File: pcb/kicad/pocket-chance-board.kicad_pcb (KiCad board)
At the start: 4 copper layers, 150 x 100 mm, 132 parts, among them J1 SWD, J2 USB4085-GF-A, J3 LiPo JST-PH 2.0mm (1 = + RED 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, J4 LCD 1.54in ST7789 module, JST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, J5 Speaker JST-PH, J6 microSD Molex 104031-0811, J7 STEMMA QT, J8 Expansion (6 = VBAT_SENSE ADC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, Q1 FS8205A, Q3 AO3400A, Q4 AO3401A, SW1 BOOT, SW10 DPAD LEFT PTS645SM43SMTR92, SW11 DPAD RIGHT PTS645SM43SMTR92, SW12 DPAD PRESS PTS645SM43SMTR92, SW2 RESET, SW3 POWER PCM12, SW4 A PTS125SM43SMTR2LFS, SW5 B PTS125SM43SMTR2LFS, SW6 X PTS125SM43SMTR2LFS, SW7 Y PTS125SM43SMTR2LFS, SW8 DPAD UP PTS645SM43SMTR92, SW9 DPAD DOWN PTS645SM43SMTR92, U1 RP2350A, U10 LSM6DSOXTR, U11 RM2, U2 W25Q128JVSIQ, U3 APS6404L-3SQR-SN, U4 USBLC6-2SC6, U5 BQ24074RGTR, U6 TPS63001DRCR, U7 DW01A, U8 PAM8302AADCR, U9 DS3231MZ+, Y1 12MHz ABM8-272-T3

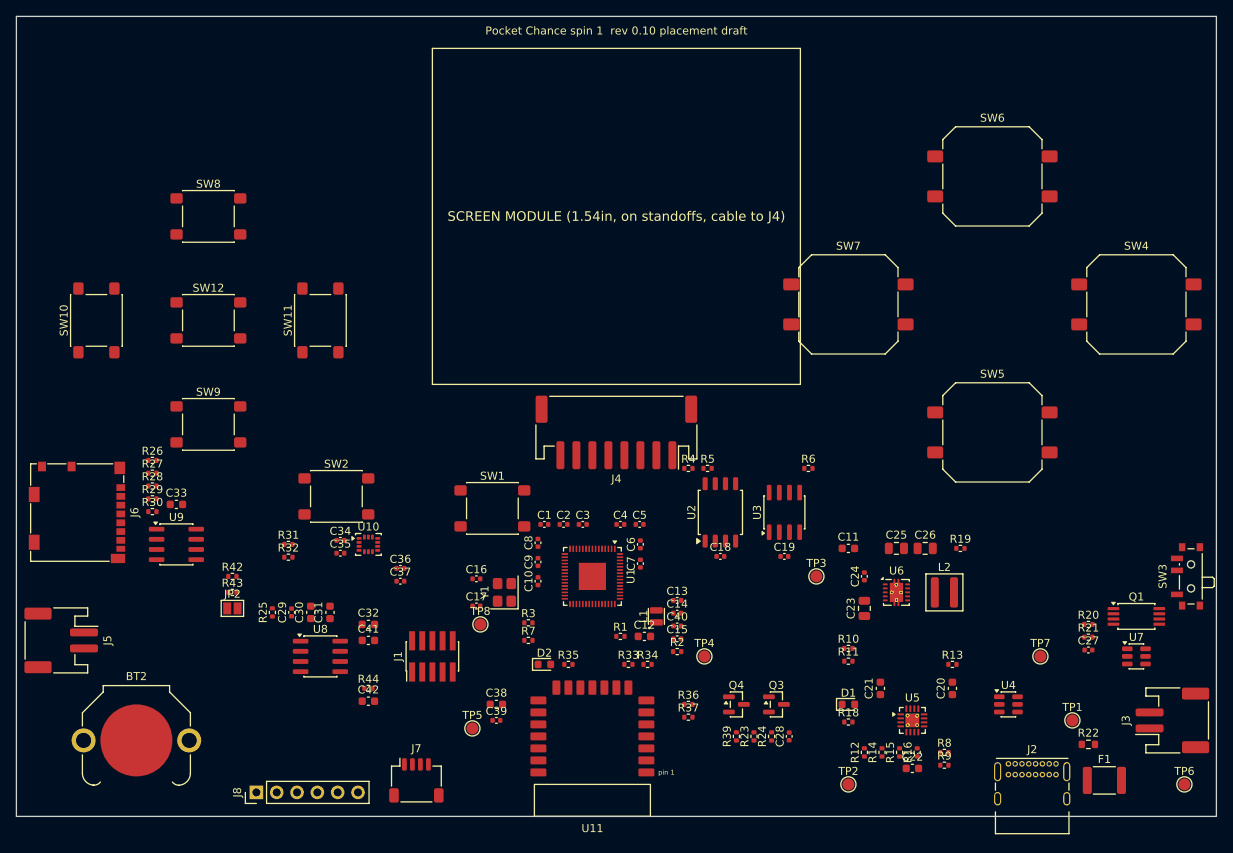
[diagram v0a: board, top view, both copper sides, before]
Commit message: Layout: placement pass 2 after the auditor's and expert's placement reviews
- RM2 keep-out rule area on all four copper layers (*.Cu), not F&B only
- U6 buck-boost repacked: L2 against the switch pins, VIN/VOUT caps on their pins
- RP2350 core regulator: L1/C13 within 1.5-2.6 mm of LX/VIN; every bypass cap at its own supply pin
- L1 orientation dot moved to pad 2 (1V1 output end), per RP2350 datasheet Figures 26 and 28
- charger caps on their pins; USB ESD next to the connector; SD and RTC bypass at their pins
- screen reserve 52 x 37 mm (fits the 50 x 35 1.54in module and the 1.3in); ABXY moved clear
- J3 '+ RED' / '- BLK' silk and meter warning; cell outline on the back; two tie-down holes
- rail names next to every test point; Bourns MF-MSMF 1812 footprint drawn (assignment waits for rev 0.11)
- generator keeps the project's net-class rules (0.15 mm) when saving
Schematic unchanged (rev 0.10, hash 897649b0).
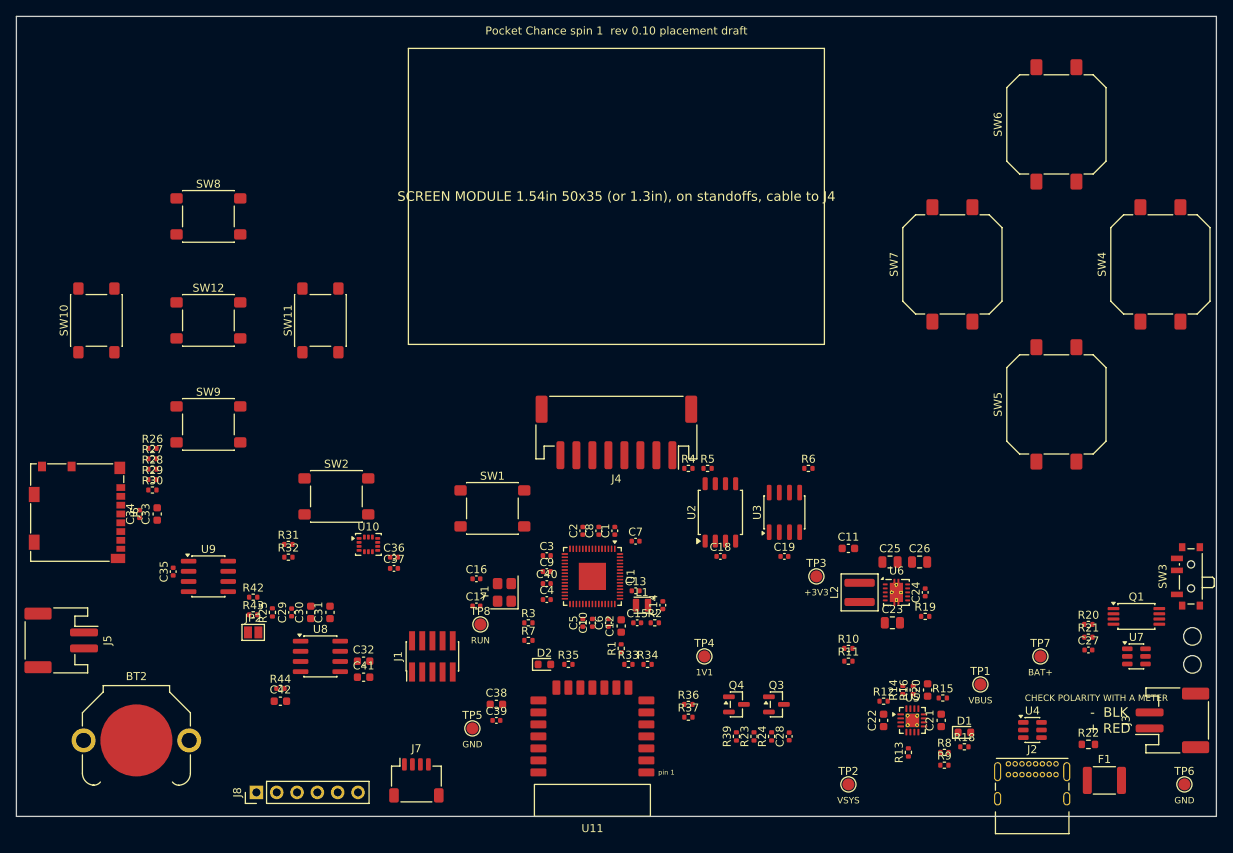
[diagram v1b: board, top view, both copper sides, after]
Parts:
- added H1: tie-down hole, , F.Cu at (197.0, 127.5)
- added H2: tie-down hole, , F.Cu at (197.0, 131.0)
- moved C34 25.3 mm to (65.4, 112.2), turned to 90 degrees
- moved C35 21.0 mm to (69.6, 119.4), turned to 90 degrees
- moved C40 17.1 mm to (116.3, 120.9)
- moved D1 14.9 mm to (168.5, 139.5)
- moved R18 14.8 mm to (168.5, 141.3)
- moved C5 14.2 mm to (120.8, 125.8), turned to 90 degrees
- moved SW7 13.9 mm to (167.0, 81.0), turned to 90 degrees
- moved C4 13.2 mm to (116.3, 122.9)
- moved TP1 12.3 mm to (170.5, 133.5)
- moved R13 12.3 mm to (161.5, 142.0), turned to 90 degrees
- moved C42 11.0 mm to (83.0, 135.6)
- moved R44 11.0 mm to (83.0, 134.0)
- moved L2 10.6 mm to (155.4, 122.0), turned to 90 degrees
- moved C6 10.6 mm to (124.0, 125.8)
- moved SW6 10.3 mm to (180.0, 63.5), turned to 90 degrees
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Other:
- board text added: "+ RED"
- board text added: "- BLK"
- board text added: "CHECK POLARITY WITH A METER"
- board text added: "LiPo CELL 52 x 34 x 10 (tape here, lead to J3 round the right edge)"
- board text added: "SCREEN MODULE 1.54in 50x35 (or 1.3in), on standoffs, cable to J4"
- board text removed: "SCREEN MODULE (1.54in, on standoffs, cable to J4)"

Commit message: Layout: no copper pour or vias under L1 on F.Cu/In1/In2; cell moved to the back of the A/B/X/Y area; routing checklist in STAGE2
Auditor 19:21: the cell outline overlapped the back of the charger and buck-boost; now behind the
buttons (SMD only, nothing hot, no through-hole tails). Auditor and expert: cut copper under the LX
inductor on inner layers too (RP2350 datasheet p.411); B.Cu keeps its ground plane as on the Pico 2.
Schematic unchanged (rev 0.10).
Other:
- board text added: "LiPo CELL 52 x 34 x 10 on insulating foam tape; lead to J3 round the right edge"
- board text removed: "LiPo CELL 52 x 34 x 10 (tape here, lead to J3 round the right edge)"

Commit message: Layout: cell label on three lines inside its outline
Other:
- board text added: "LiPo CELL 52 x 34 x 10"
- board text added: "lead to J3 round the right edge"
- board text added: "on insulating foam tape"
- board text removed: "LiPo CELL 52 x 34 x 10 on insulating foam tape; lead to J3 round the right edge"

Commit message: Layout: 3.0 mm tie-down holes, four M2 corner mounting holes, speaker 'not GND' silk (auditor off-board list 19:28)
Cell outline shifted to x 92-144 and TP6 moved to clear the corner holes. Schematic unchanged.
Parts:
- added MH1: tie-down hole, , F.Cu at (53.5, 53.5)
- added MH2: tie-down hole, , F.Cu at (196.5, 53.5)
- added MH3: tie-down hole, , F.Cu at (53.5, 146.5)
- added MH4: tie-down hole, , F.Cu at (196.5, 146.5)
- moved TP6 4.27 mm to (192.0, 147.5)
- moved H1 1.00 mm to (197.0, 126.5)
- moved H2 0.20 mm to (197.0, 131.2)
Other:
- board text added: "SPK+ SPK-: bridge output,"
- board text added: "neither wire is GND"
